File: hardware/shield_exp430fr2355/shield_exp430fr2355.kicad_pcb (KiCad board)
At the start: 2 copper layers, 78.4 x 50 mm, 50 parts, among them J1 TI_BOOSTER_40_J1, J10 Conn_01x02_Male, J12 Conn_01x02_Male, J13 Conn_01x02_Male, J14 Conn_01x02_Male, J15 Conn_01x02_Male, J16 Conn_01x02_Male, J17 Conn_01x02_Male, J18 Conn_01x02_Male, J19 Conn_01x02_Male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

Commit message: Added diode
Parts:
- added D8: D_Schottky, Diode_SMD:D_SMB, B.Cu at (200.0, 130.2)
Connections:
- J6 pad 15: +5V -> +5VP
- J6 pad 16: +5V -> +5VP
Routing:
- net +5V: track 57.2 -> 13.8 mm
- net +5VP: track 0.00 -> 41.6 mm
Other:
- board text added: "3V3 POWER"
- board text removed: "POWER"
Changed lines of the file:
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@@
     (thickness 1.6)
     (drawings 31)
-    (tracks 644)
+    (tracks 646)
     (zones 0)
-    (modules 50)
-    (nets 68)
+    (modules 51)
+    (nets 69)
   )
   (page A3)
@@
   (net 66 P4.0)
   (net 67 "Net-(J6-Pad18)")
+  (net 68 +5VP)
   (net_class Default "This is the default net class."
     (clearance 0.3048)
@@
     (diff_pair_width 0.254)
     (add_net +3V3)
+    (add_net +5VP)
     (add_net ADC0)
     (add_net ADC1)
@@
     (add_net +5V)
   )
+  (module Diode_SMD:D_SMB (layer B.Cu)
+    (at 199.9742 130.1623 90)
+    (descr "Diode SMB (DO-214AA)")
+    (tags "Diode SMB (DO-214AA)")
+    (attr smd)
+    (fp_text reference D8 (at 0 3 90) (layer B.SilkS)
+      (effects (font (size 1 1) (thickness 0.15)) (justify mirror))
+    )
+    (fp_text value D_Schottky (at 0 -3.1 90) (layer B.Fab)
+      (effects (font (size 1 1) (thickness 0.15)) (justify mirror))
+    )
+    (fp_text user %R (at 0 3 90) (layer B.Fab)
+      (effects (font (size 1 1) (thickness 0.15)) (justify mirror))
+    )
+    (fp_line (start -3.55 2.15) (end -3.55 -2.15) (layer B.SilkS) (width 0.12))
+    (fp_line (start 2.3 -2) (end -2.3 -2) (layer B.Fab) (width 0.1))
+    (fp_line (start -2.3 -2) (end -2.3 2) (layer B.Fab) (width 0.1))
+    (fp_line (start 2.3 2) (end 2.3 -2) (layer B.Fab) (width 0.1))
+    (fp_line (start 2.3 2) (end -2.3 2) (layer B.Fab) (width 0.1))
+    (fp_line (start -3.65 2.25) (end 3.65 2.25) (layer B.CrtYd) (width 0.05))
+    (fp_line (start 3.65 2.25) (end 3.65 -2.25) (layer B.CrtYd) (width 0.05))
+    (fp_line (start 3.65 -2.25) (end -3.65 -2.25) (layer B.CrtYd) (width 0.05))
+    (fp_line (start -3.65 -2.25) (end -3.65 2.25) (layer B.CrtYd) (width 0.05))
+    (fp_line (start -0.64944 -0.00102) (end -1.55114 -0.00102) (layer B.Fab) (width 0.1))
+    (fp_line (start 0.50118 -0.00102) (end 1.4994 -0.00102) (layer B.Fab) (width 0.1))
+    (fp_line (start -0.64944 0.79908) (end -0.64944 -0.80112) (layer B.Fab) (width 0.1))
+    (fp_line (start 0.50118 -0.75032) (end 0.50118 0.79908) (layer B.Fab) (width 0.1))
+    (fp_line (start -0.64944 -0.00102) (end 0.50118 -0.75032) (layer B.Fab) (width 0.1))
+    (fp_line (start -0.64944 -0.00102) (end 0.50118 0.79908) (layer B.Fab) (width 0.1))
+    (fp_line (start -3.55 -2.15) (end 2.15 -2.15) (layer B.SilkS) (width 0.12))
+    (fp_line (start -3.55 2.15) (end 2.15 2.15) (layer B.SilkS) (width 0.12))
+    (pad 1 smd rect (at -2.15 0 90) (size 2.5 2.3) (layers B.Cu B.Paste B.Mask)
+      (net 2 +5V))
+    (pad 2 smd rect (at 2.15 0 90) (size 2.5 2.3) (layers B.Cu B.Paste B.Mask)
+      (net 68 +5VP))
+    (model ${KISYS3DMOD}/Diode_SMD.3dshapes/D_SMB.wrl
+      (at (xyz 0 0 0))
+      (scale (xyz 1 1 1))
+      (rotate (xyz 0 0 0))
+    )
+  )
   (module Package_TO_SOT_SMD:SOT-23 (layer B.Cu)
     (at 188.29 153.02)
@@
       (net 18 L_TCRT))
     (pad 15 thru_hole rect (at 0 17.78) (size 2 2) (drill 1) (layers *.Cu *.Mask)
-      (net 2 +5V))
+      (net 68 +5VP))
     (pad 16 thru_hole rect (at -2.54 17.78) (size 2 2) (drill 1) (layers *.Cu *.Mask)
-      (net 2 +5V))
+      (net 68 +5VP))
     (pad 17 thru_hole rect (at 0 20.32) (size 2 2) (drill 1) (layers *.Cu *.Mask)
       (net 19 TXB))
@@
     (effects (font (size 1 1) (thickness 0.1)))
   )
-  (gr_text POWER (at 187.02 143.55) (layer F.SilkS)
+  (gr_text "3V3\nPOWER" (at 186.9948 144.0561) (layer F.SilkS)
     (effects (font (size 1 1) (thickness 0.1)))
   )
@@
   (segment (start 208.7064 130.8444) (end 208.901 131.039) (width 0.7) (layer B.Cu) (net 2))
   (segment (start 206.2988 130.8444) (end 208.7064 130.8444) (width 0.7) (layer B.Cu) (net 2))
-  (segment (start 178.2318 151.1046) (end 180.7718 151.1046) (width 0.7) (layer B.Cu) (net 2))
+  (segment (start 178.2318 151.1046) (end 180.7718 151.1046) (width 0.7) (layer B.Cu) (net 68))
   (segment (start 199.925053 134.534947) (end 199.925053 131.78217) (width 0.7) (layer B.Cu) (net 2))
   (segment (start 199.92 134.54) (end 199.925053 134.534947) (width 0.7) (layer B.Cu) (net 2))
   (segment (start 199.92 136.09) (end 199.92 134.54) (width 0.7) (layer B.Cu) (net 2))
-  (segment (start 180.7718 151.1046) (end 181.973881 151.1046) (width 0.7) (layer B.Cu) (net 2))
-  (segment (start 183.828081 150.321919) (end 183.0454 151.1046) (width 0.7) (layer B.Cu) (net 2))
-  (segment (start 183.828081 149.019659) (end 183.828081 150.321919) (width 0.7) (layer B.Cu) (net 2))
-  (segment (start 187.20414 145.6436) (end 183.828081 149.019659) (width 0.7) (layer B.Cu) (net 2))
-  (segment (start 191.643 145.6436) (end 187.20414 145.6436) (width 0.7) (layer B.Cu) (net 2))
-  (segment (start 199.925053 129.694053) (end 199.263 129.032) (width 0.7) (layer B.Cu) (net 2))
-  (segment (start 199.263 129.032) (end 194.0433 129.032) (width 0.7) (layer B.Cu) (net 2))
-  (segment (start 199.925053 131.78217) (end 199.925053 129.694053) (width 0.7) (layer B.Cu) (net 2))
-  (segment (start 192.41059 144.87601) (end 191.643 145.6436) (width 0.7) (layer B.Cu) (net 2))
-  (segment (start 194.0433 129.032) (end 192.405 130.6703) (width 0.7) (layer B.Cu) (net 2))
-  (segment (start 183.0454 151.1046) (end 180.7718 151.1046) (width 0.7) (layer B.Cu) (net 2))
-  (segment (start 192.405 130.6703) (end 192.405 144.87042) (width 0.7) (layer B.Cu) (net 2))
-  (segment (start 192.405 144.87042) (end 192.41059 144.87601) (width 0.7) (layer B.Cu) (net 2))
+  (segment (start 180.7718 151.1046) (end 181.973881 151.1046) (width 0.7) (layer B.Cu) (net 68))
+  (segment (start 183.828081 150.321919) (end 183.0454 151.1046) (width 0.7) (layer B.Cu) (net 68))
+  (segment (start 183.828081 149.019659) (end 183.828081 150.321919) (width 0.7) (layer B.Cu) (net 68))
+  (segment (start 187.20414 145.6436) (end 183.828081 149.019659) (width 0.7) (layer B.Cu) (net 68))
+  (segment (start 191.643 145.6436) (end 187.20414 145.6436) (width 0.7) (layer B.Cu) (net 68))
+  (segment (start 192.41059 144.87601) (end 191.643 145.6436) (width 0.7) (layer B.Cu) (net 68))
+  (segment (start 194.0433 129.032) (end 192.405 130.6703) (width 0.7) (layer B.Cu) (net 68))
+  (segment (start 183.0454 151.1046) (end 180.7718 151.1046) (width 0.7) (layer B.Cu) (net 68))
+  (segment (start 192.405 130.6703) (end 192.405 144.87042) (width 0.7) (layer B.Cu) (net 68))
+  (segment (start 192.405 144.87042) (end 192.41059 144.87601) (width 0.7) (layer B.Cu) (net 68))
   (segment (start 211.201 126.247) (end 211.201 131.039) (width 0.508) (layer B.Cu) (net 3))
   (segment (start 211.201 124.739) (end 211.201 126.247) (width 0.508) (layer B.Cu) (net 3))
@@
   (segment (start 246.72 159.58) (end 246.72 161.53) (width 0.508) (layer B.Cu) (net 61))
   (segment (start 246.07 158.93) (end 246.72 159.58) (width 0.508) (layer B.Cu) (net 61))
+  (segment (start 197.2965 129.032) (end 197.3092 129.0447) (width 0.508) (layer B.Cu) (net 68))
+  (segment (start 194.0433 129.032) (end 197.2965 129.032) (width 0.7) (layer B.Cu) (net 68))
+  (segment (start 198.3162 128.0123) (end 199.9742 128.0123) (width 0.7) (layer B.Cu) (net 68))
+  (segment (start 197.3092 129.0193) (end 198.3162 128.0123) (width 0.7) (layer B.Cu) (net 68))
+  (segment (start 197.3092 129.0447) (end 197.3092 129.0193) (width 0.508) (layer B.Cu) (net 68))
   (zone (net 1) (net_name GND) (layer B.Cu) (hatch edge 0.508)
     (connect_pads (clearance 0.508))

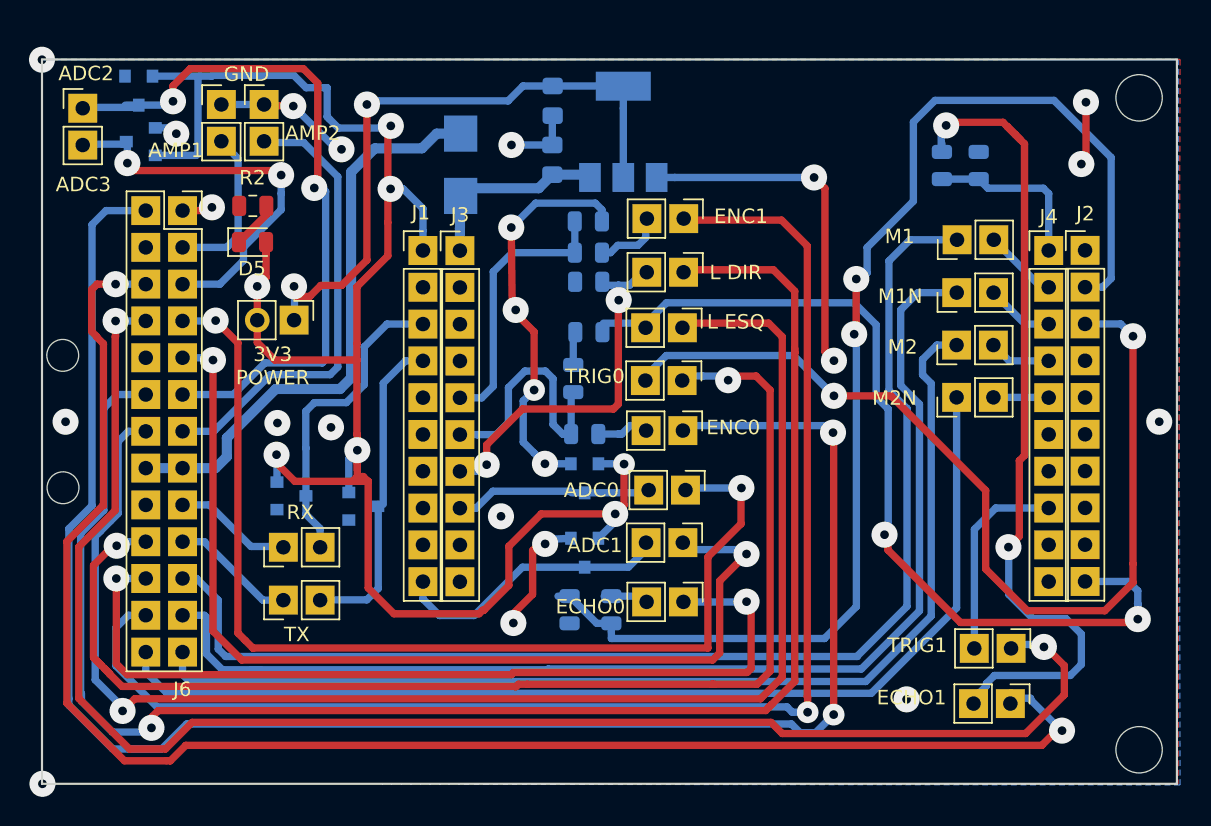
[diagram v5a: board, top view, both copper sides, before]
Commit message: Change 26 via connector
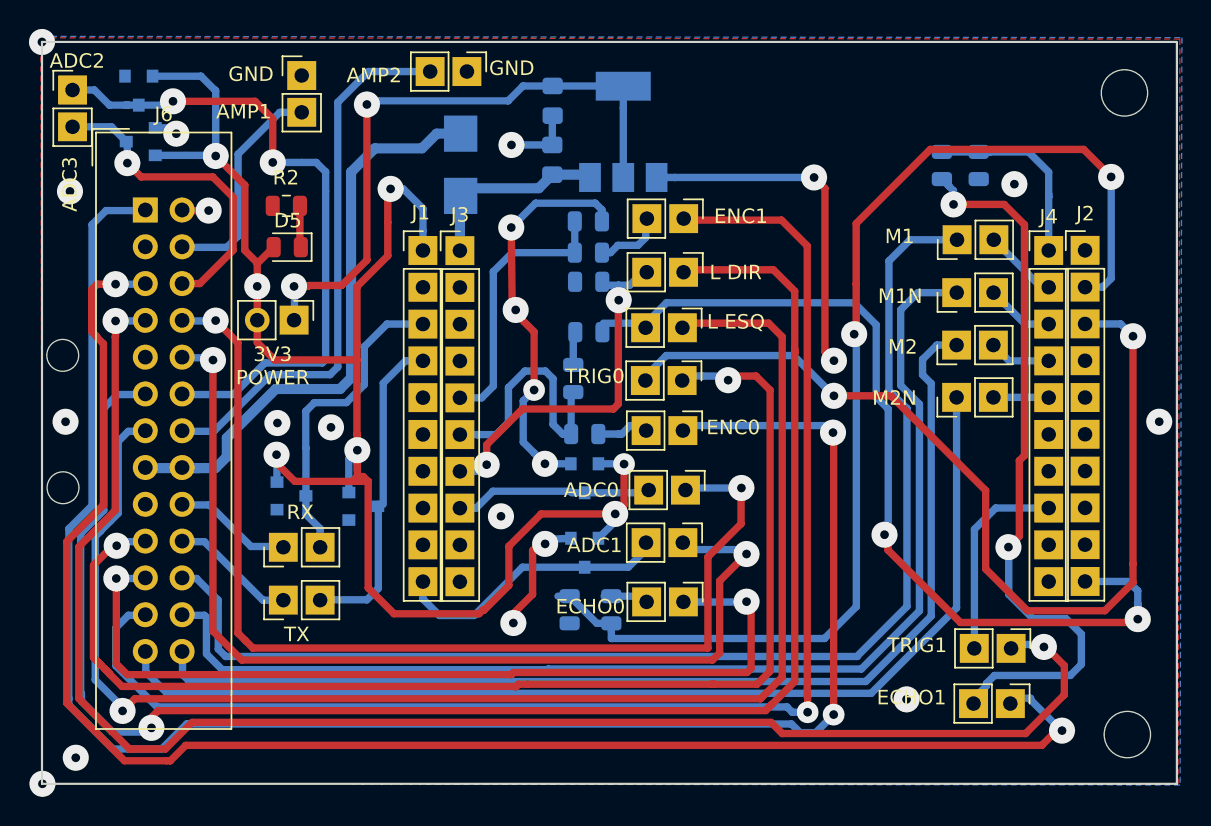
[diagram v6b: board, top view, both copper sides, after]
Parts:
- J6: footprint Connector_PinSocket_2.54mm:PinSocket_2x13_P2.54mm_Vertical -> Connector_IDC:IDC-Header_2x13_P2.54mm_Vertical
- R10, R11, R3, R5: value 20K -> 15k
- R2: value R -> 820R
- R8, R9: value 20K -> 15K
- moved J10 14.2 mm to (200.4, 123.7), turned to 270 degrees
- moved J9 5.90 mm to (189.0, 124.0)
- moved J6 2.57 mm to (178.2, 133.3)
- moved D5 2.43 mm to (188.0, 135.8), turned to 180 degrees
- moved R2 2.32 mm to (187.9, 133.0)
- moved J8 1.44 mm to (173.2, 125.0)
- moved H3 1.33 mm to (246.0, 169.5)
- moved H4 1.07 mm to (245.8, 125.2)
- turned R4 to 90 degrees
- turned R5 to 270 degrees
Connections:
- J6 pad 1: GND -> D0
- J6 pad 10: Net-(J6-Pad10) -> ADC1
- J6 pad 11: ADC2 -> R_TCRT
- J6 pad 12: R_TCRT -> ADC2
- J6 pad 13: AMP2 -> L_TCRT
- J6 pad 14: L_TCRT -> AMP2
- J6 pad 17: TXB -> Net-(J6-Pad17)
- J6 pad 18: Net-(J6-Pad18) -> TXB
- J6 pad 19: RXB -> Trig0
- J6 pad 2: D0 -> GND
- J6 pad 20: Trig0 -> RXB
- J6 pad 21: PWM1 -> Echo0
- J6 pad 22: Echo0 -> PWM1
- J6 pad 23: PWM1N -> D1
- J6 pad 24: D1 -> PWM1N
- J6 pad 25: PWM2 -> PWM2N
- J6 pad 26: PWM2N -> PWM2
- J6 pad 3: AMP1 -> GND
- J6 pad 4: GND -> AMP1
- J6 pad 5: ADC3 -> Echo1
- J6 pad 6: Echo1 -> ADC3
- J6 pad 7: ADC0 -> Trig1
- J6 pad 8: Trig1 -> ADC0
- J6 pad 9: ADC1 -> Net-(J6-Pad9)
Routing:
- net GND: track 85.5 -> 72.0 mm, vias 20 -> 19
- net +3V3: track 126.2 -> 115.6 mm
- net Net-(J19-Pad2): track 58.6 -> 50.3 mm
- net AMP2: track 31.7 -> 38.1 mm
- net P2.0: track 84.7 -> 79.4 mm
- net ADC3: track 27.4 -> 22.7 mm, vias 2 -> 1
- net AMP1: track 11.0 -> 15.4 mm
- net ADC2: track 49.5 -> 46.0 mm
- net P2.1: track 11.7 -> 14.5 mm
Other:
- board size 78.4 x 50 mm -> 78.4 x 51.2 mm

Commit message: Added board info
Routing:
- net (no net): vias 3 -> 1
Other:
- board text added: "Shield EXP430FR2355 Prof. Renan Augusto Starke"
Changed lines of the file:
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@@
   (general
     (thickness 1.6)
-    (drawings 31)
-    (tracks 629)
+    (drawings 32)
+    (tracks 627)
     (zones 0)
     (modules 51)
@@
     (visible_elements 7FFFFFFF)
     (pcbplotparams
-      (layerselection 0x01000_ffffffff)
+      (layerselection 0x01030_ffffffff)
       (usegerberextensions true)
       (usegerberattributes false)
@@
       (drillshape 0)
       (scaleselection 1)
-      (outputdirectory "gerber/"))
+      (outputdirectory "fabric/"))
   )
   (net 0 "")
@@
     )
   )
+  (gr_text "Shield EXP430FR2355\nProf. Renan Augusto Starke" (at 227.33 124.46) (layer F.SilkS)
+    (effects (font (size 1 1) (thickness 0.1)))
+  )
   (gr_text GND (at 203.5 123.5) (layer F.SilkS)
     (effects (font (size 1 1) (thickness 0.1)))
@@
   (gr_line (start 171.069 172.8978) (end 171.069 121.67616) (angle 90) (layer Edge.Cuts) (width 0.14986))
   (gr_line (start 249.42 121.68124) (end 249.42 172.9) (angle 90) (layer Edge.Cuts) (width 0.14986))
-  (via (at 171.1 172.9) (size 1.8) (drill 0.6) (layers F.Cu B.Cu) (net 0))
   (via (at 172.6946 147.9042) (size 1.8) (drill 0.6) (layers F.Cu B.Cu) (net 0))
-  (via (at 171.069 121.68632) (size 1.8) (drill 0.6) (layers F.Cu B.Cu) (net 0))
   (via (at 180.34 128.016) (size 1.8) (drill 0.6) (layers F.Cu B.Cu) (net 1))
   (segment (start 178.8889 127.6121) (end 180.1767 127.6121) (width 0.508) (layer B.Cu) (net 1))
@@
   (segment (start 212.6511 159.9461) (end 213.0552 160.3502) (width 0.508) (layer B.Cu) (net 27))
   (segment (start 210.3755 159.9461) (end 212.6511 159.9461) (width 0.508) (layer B.Cu) (net 27))
+  (segment (start 233.1466 129.2248) (end 233.1974 129.2756) (width 0.508) (layer B.Cu) (net 29))
+  (segment (start 233.1974 129.2756) (end 235.7374 129.2756) (width 0.508) (layer B.Cu) (net 29))
+  (segment (start 236.5374 129.2756) (end 235.7374 129.2756) (width 0.508) (layer B.Cu) (net 29))
+  (segment (start 235.7374 129.2756) (end 239.1756 129.2756) (width 0.508) (layer B.Cu) (net 29))
+  (segment (start 240.57 130.67) (end 240.57 132.4) (width 0.508) (layer B.Cu) (net 29))
+  (segment (start 239.1756 129.2756) (end 240.57 130.67) (width 0.508) (layer B.Cu) (net 29))
+  (segment (start 240.57 136.08) (end 240.57 132.4) (width 0.508) (layer B.Cu) (net 29))
+  (segment (start 240.57 132.4) (end 240.57 132.15217) (width 0.508) (layer B.Cu) (net 29))
   (via (at 225.7425 146.1135) (size 1.8) (drill 0.6) (layers F.Cu B.Cu) (net 30))
   (segment (start 222.974799 143.345799) (end 225.7425 146.1135) (width 0.508) (layer B.Cu) (net 30))
@@
   (segment (start 236.91 153.86) (end 240.57 153.86) (width 0.508) (layer B.Cu) (net 31))
   (segment (start 235.44 155.33) (end 236.91 153.86) (width 0.508) (layer B.Cu) (net 31))
-  (segment (start 233.1466 129.2248) (end 233.1974 129.2756) (width 0.508) (layer B.Cu) (net 29))
-  (segment (start 233.1974 129.2756) (end 235.7374 129.2756) (width 0.508) (layer B.Cu) (net 29))
-  (segment (start 236.5374 129.2756) (end 235.7374 129.2756) (width 0.508) (layer B.Cu) (net 29))
-  (segment (start 235.7374 129.2756) (end 239.1756 129.2756) (width 0.508) (layer B.Cu) (net 29))
-  (segment (start 240.57 130.67) (end 240.57 132.4) (width 0.508) (layer B.Cu) (net 29))
-  (segment (start 239.1756 129.2756) (end 240.57 130.67) (width 0.508) (layer B.Cu) (net 29))
-  (segment (start 240.57 136.08) (end 240.57 132.4) (width 0.508) (layer B.Cu) (net 29))
-  (segment (start 240.57 132.4) (end 240.57 132.15217) (width 0.508) (layer B.Cu) (net 29))
   (via (at 237.79 156.56) (size 1.8) (drill 0.6) (layers F.Cu B.Cu) (net 33))
   (segment (start 236.269999 166.140001) (end 235.42 166.99) (width 0.508) (layer B.Cu) (net 33))
